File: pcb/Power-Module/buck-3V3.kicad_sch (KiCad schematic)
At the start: 11 parts, among them U1 TPS562202

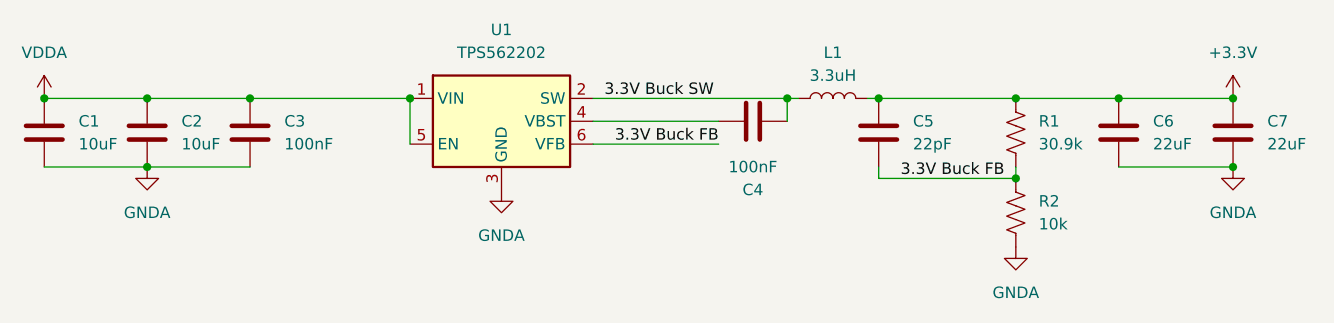
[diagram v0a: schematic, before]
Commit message: 12V and 3.3V supplies in correct form factor
Completed layout of 3.3V out buck converter and 12V out SEPIC converter. Layout fits on board with the same shape and hole pattern as the rev 1 Ride-Along Module.
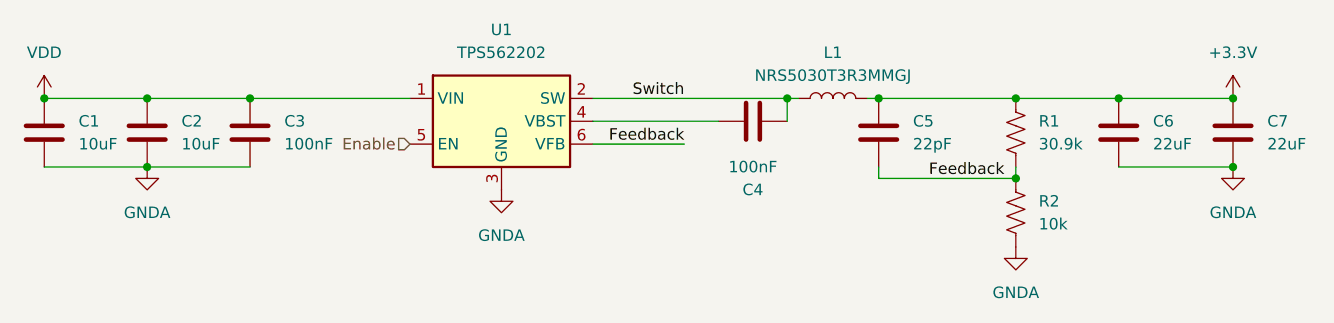
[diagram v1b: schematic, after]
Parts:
- L1: value 3.3uH -> NRS5030T3R3MMGJ; footprint Inductor_SMD:L_0603_1608Metric_Pad1.05x0.95mm_HandSolder -> Inductor_SMD:L_Taiyo-Yuden_NR-50xx_HandSoldering
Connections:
- net 3.3V Buck FB renamed Feedback
- net 3.3V Buck SW renamed Switch
- net VDDA renamed VDD
- net VDD: no longer U1.5 (EN)
- new net Enable: U1.5 (EN)
